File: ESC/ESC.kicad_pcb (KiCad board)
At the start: 4 copper layers, 75.6 x 63 mm, 93 parts, among them J1 Conn_01x02_Socket, J2 Conn_01x03, J3 Conn_01x03, J4 swd, J5 input, Q1 BSC028N06LS3, Q10 BSC028N06LS3, Q11 BSC028N06LS3, Q12 BSC028N06LS3, Q2 BSC028N06LS3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

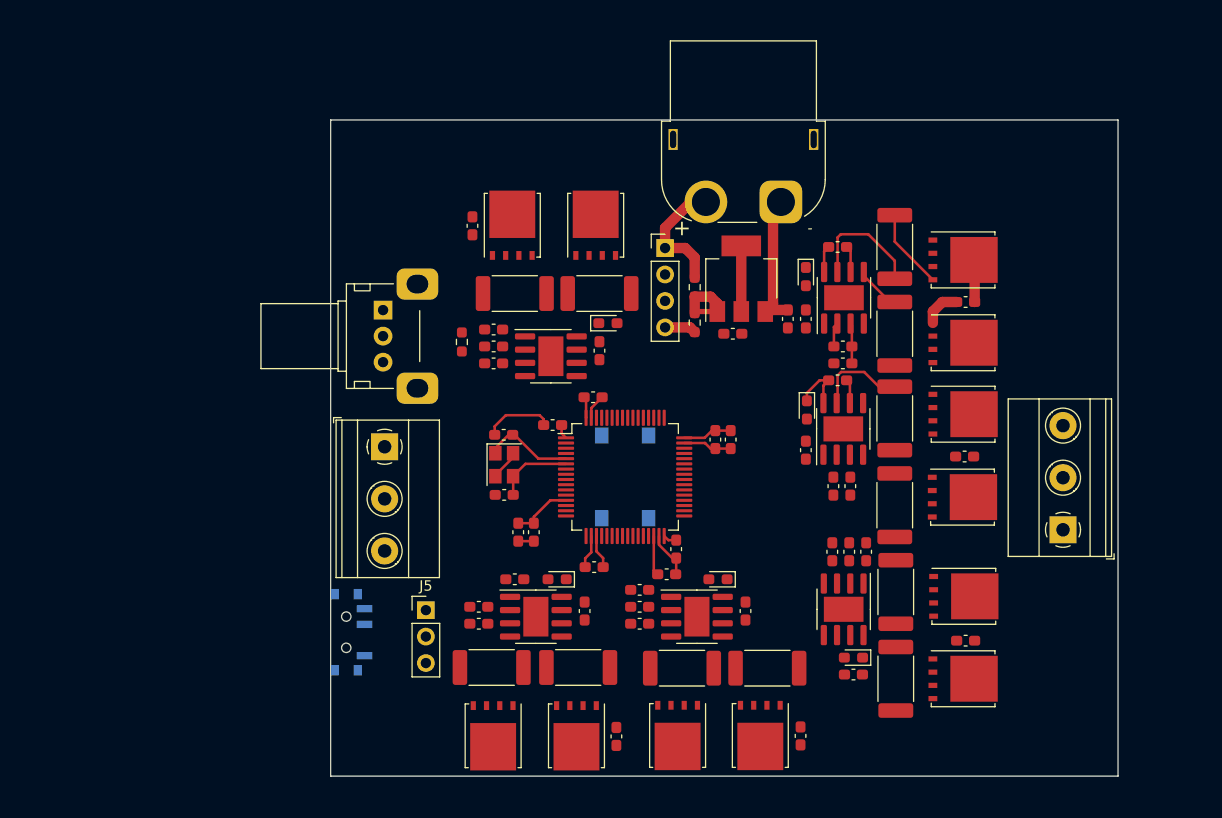
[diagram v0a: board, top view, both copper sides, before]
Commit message: did some of the routing ofthe PCB
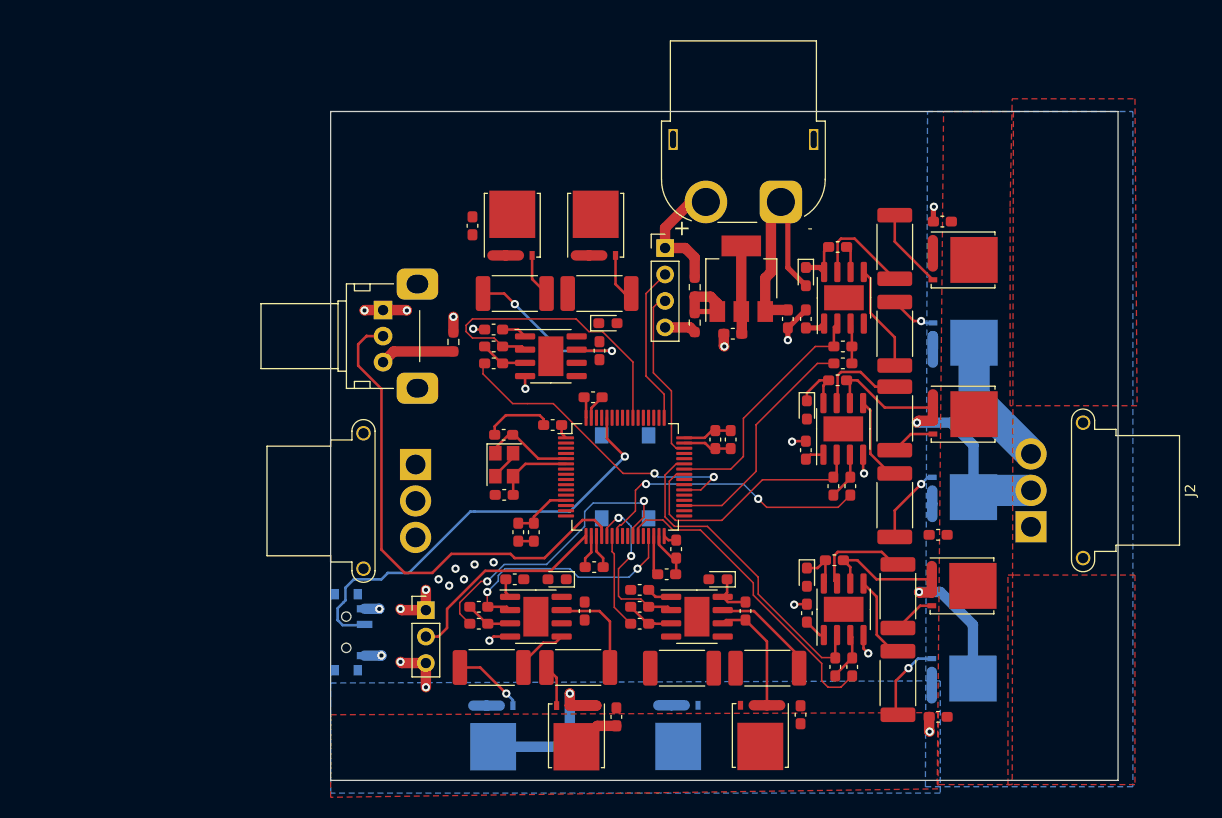
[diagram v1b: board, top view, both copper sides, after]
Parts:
- J2, J3: footprint TerminalBlock_Phoenix:TerminalBlock_Phoenix_MKDS-1,5-3_1x03_P5.00mm_Horizontal -> Connector_AMASS:AMASS_MR30PW-FB_1x03_P3.50mm_Horizontal
- Q12, Q2, Q4, Q6, Q8: moved to B.Cu
- moved C23 11.1 mm to (213.6, 110.9), turned to 0 degrees
- moved JP3 11.1 mm to (213.6, 121.2)
- moved JP5 11.1 mm to (215.3, 121.2)
- moved D3 8.92 mm to (210.9, 112.6), turned to -90 degrees
- moved Q5 8.92 mm to (225.8, 113.4)
- moved R8 8.74 mm to (219.7, 122.7)
- moved C21 8.19 mm to (210.9, 116.0)
- moved C19 8.04 mm to (223.9, 78.4)
- moved C15 7.94 mm to (223.5, 108.5)
- moved R7 7.93 mm to (219.7, 114.4)
- moved Q6 7.89 mm to (225.8, 122.3)
- moved C22 7.78 mm to (223.5, 126.0)
- moved J3 3.43 mm to (173.4, 101.8), turned to 90 degrees
- moved J2 3.09 mm to (232.4, 107.7), turned to -90 degrees
- moved C25 2.03 mm to (210.3, 125.8)
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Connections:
- R6 pad 1: Net-(U6-LO) -> Net-(Q2-G)
- R6 pad 2: Net-(Q2-G) -> Net-(U6-LO)
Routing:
- net /ADC1_IN4: track 0.00 -> 49.0 mm
- net Net-(SW1-B): track 0.00 -> 42.7 mm, vias 0 -> 1
- net GND: track 42.0 -> 83.5 mm, vias 0 -> 22
- net TIM1_CH3: track 0.00 -> 31.5 mm
- net TIM3_CH2: track 0.00 -> 30.7 mm, vias 0 -> 2
- net Net-(J2-Pin_2): track 2.32 -> 32.9 mm, vias 0 -> 1
- net TIM1_CH3N: track 0.00 -> 30.4 mm
- net TIM2_CH2: track 0.00 -> 30.3 mm
- net TIM3_CH3: track 0.00 -> 28.8 mm, vias 0 -> 2
- net TIM1_CH1N: track 0.00 -> 27.5 mm, vias 0 -> 2
- net Net-(J2-Pin_1): track 0.00 -> 27.2 mm, vias 0 -> 1
- net TIM1_CH1: track 0.00 -> 24.9 mm
- net TIM2_CH3: track 0.00 -> 24.1 mm, vias 0 -> 2
- net TIM1_CH2N: track 0.00 -> 22.6 mm
- net VCC: track 17.7 -> 40.0 mm
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- added copper zone on In2.Cu, net +3.3V
- added copper zone on B.Cu, net GND
- added copper zone on In1.Cu, net GND
- added copper zone on F.Cu, net VCC
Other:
- board size 75.6 x 63 mm -> 75.6 x 64.2 mm

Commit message: finished the pcb layout of the ESC and now need to be revised to make sure everything is correct
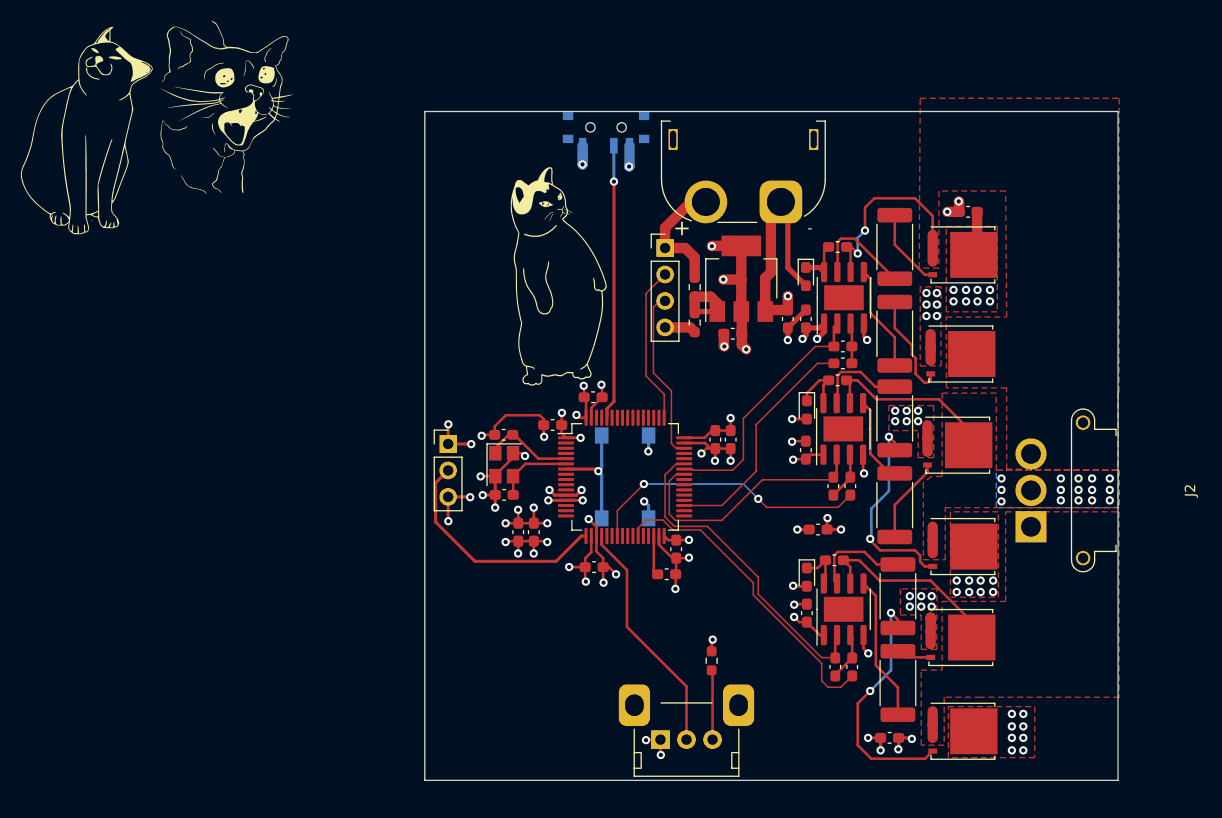
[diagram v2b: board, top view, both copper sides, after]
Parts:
- removed C24, C27, C30: 100n 50V, Capacitor_SMD:C_0603_1608Metric_Pad1.08x0.95mm_HandSolder
- removed C25, C28, C31: 4u7, Capacitor_SMD:C_0603_1608Metric_Pad1.08x0.95mm_HandSolder
- removed C26, C29, C32: 2u7 50V, Capacitor_SMD:C_0603_1608Metric_Pad1.08x0.95mm_HandSolder
- removed D4, D5, D6: D, Diode_SMD:D_0603_1608Metric_Pad1.05x0.95mm_HandSolder
- removed J3: Conn_01x03, Connector_AMASS:AMASS_MR30PW-FB_1x03_P3.50mm_Horizontal
- removed JP10, JP11, JP12, JP7, JP8, JP9: jump, Capacitor_SMD:C_0603_1608Metric_Pad1.08x0.95mm_HandSolder
- removed Q10, Q11, Q12, Q7, Q8, Q9: BSC028N06LS3, Package_TO_SOT_SMD:TDSON-8-1
- removed R10, R11, R12, R13, R14, R15: 200, Resistor_SMD:R_2512_6332Metric_Pad1.40x3.35mm_HandSolder
- removed U10, U8, U9: IRS2101, Package_SO:SOIC-8-1EP_3.9x4.9mm_P1.27mm_EP2.41x3.81mm
- added G***: LOGO, LOGO, F.Cu at (141.8, 69.7)
- added G***: LOGO, LOGO, F.Cu at (155.0, 67.7)
- added G***: LOGO, LOGO, F.Cu at (186.5, 83.3)
- added G***: LOGO, LOGO, B.Cu at (130.8, 90.2)
- Q2, Q4, Q6: moved to F.Cu
- moved SW1 54.1 mm to (191.6, 69.7), turned to 0 degrees
- moved RV1 49.1 mm to (196.9, 128.2), turned to 90 degrees
- moved R9 39.4 mm to (201.8, 120.6)
- moved J5 16.1 mm to (176.5, 99.8)
- moved Q5 14.0 mm to (225.9, 127.4)
- moved Q3 12.7 mm to (225.9, 109.6)
- moved C15 11.5 mm to (212.0, 108.0), turned to 0 degrees
- moved C22 5.08 mm to (218.9, 128.0)
- moved Q4 5.01 mm to (225.4, 99.9)
- moved Q6 3.94 mm to (225.7, 118.4)
- moved C19 2.64 mm to (226.4, 77.5)
- moved Q2 1.10 mm to (225.7, 91.2)
- moved Q1 0.48 mm to (225.9, 81.6)
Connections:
- net Net-(J2-Pin_1) renamed /MosFet TIM_1/TIM1_O3
- net Net-(J2-Pin_2) renamed /MosFet TIM_1/TIM1_O1
- net Net-(J2-Pin_3) renamed /MosFet TIM_1/TIM1_O2
- R8 pad 1: Net-(U7-LO) -> Net-(Q6-G)
- R8 pad 2: Net-(Q6-G) -> Net-(U7-LO)
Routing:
- net TIM3_CH2: track 30.7 -> 0.00 mm, vias 2 -> 0
- net TIM2_CH2: track 30.3 -> 0.00 mm
- net TIM3_CH3: track 28.8 -> 0.00 mm, vias 2 -> 0
- net /ADC1_IN4: track 49.0 -> 22.9 mm
- net TIM2_CH3: track 24.1 -> 0.00 mm, vias 2 -> 0
- net GND: track 83.5 -> 106.6 mm, vias 22 -> 58
- net +3.3V: track 37.9 -> 60.4 mm, vias 4 -> 22
- net Net-(Q5-G): track 4.14 -> 23.8 mm, vias 0 -> 2
- net Net-(J3-Pin_2): track 18.4 -> 0.00 mm, vias 1 -> 0
- net Net-(U9-HO): track 18.1 -> 0.00 mm, vias 2 -> 0
- net TIM2_CH1: track 16.7 -> 0.00 mm, vias 2 -> 0
- net Net-(SW1-B): track 42.7 -> 26.4 mm
- net Net-(Q3-G): track 4.30 -> 19.6 mm, vias 0 -> 2
- net Net-(J3-Pin_3): track 13.9 -> 0.00 mm
- net /MosFet TIM_1/TIM1_O1: track 32.9 -> 20.1 mm, vias 1 -> 15
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- added copper zone on B.Cu, net /MosFet TIM_1/TIM1_O1
- added copper zone on F.Cu, net /MosFet TIM_1/TIM1_O1
- added copper zone on F.Cu, net /MosFet TIM_1/TIM1_O2
- added copper zone on F.Cu, net /MosFet TIM_1/TIM1_O3
- added copper zone on F.Cu, net GND
- added copper zone on In2.Cu, net VCC
- removed copper zone on B.Cu, net GND
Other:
- board size 75.6 x 64.2 mm -> 66.5 x 64.2 mm
